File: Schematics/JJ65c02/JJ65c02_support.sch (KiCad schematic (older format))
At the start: 14 parts, among them SW1 RESET, U1 NE555, U2 74HC00, U3 74HC138, U4 74HC08, X1 1Mhz, X2 1.8Mhz

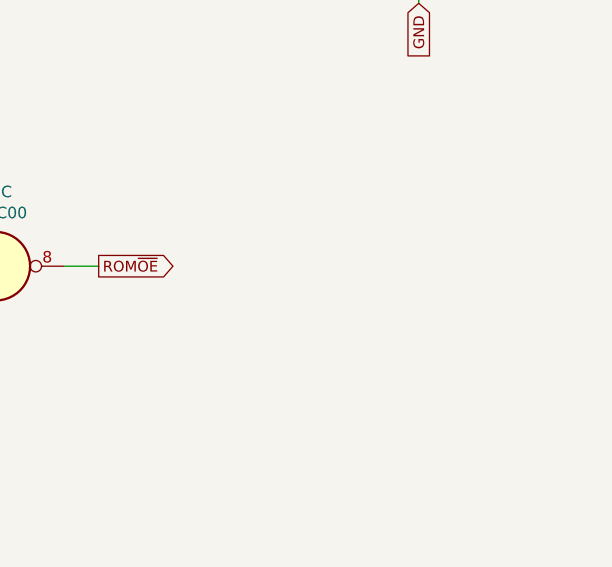
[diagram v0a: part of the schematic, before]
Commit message: Add in max232 board
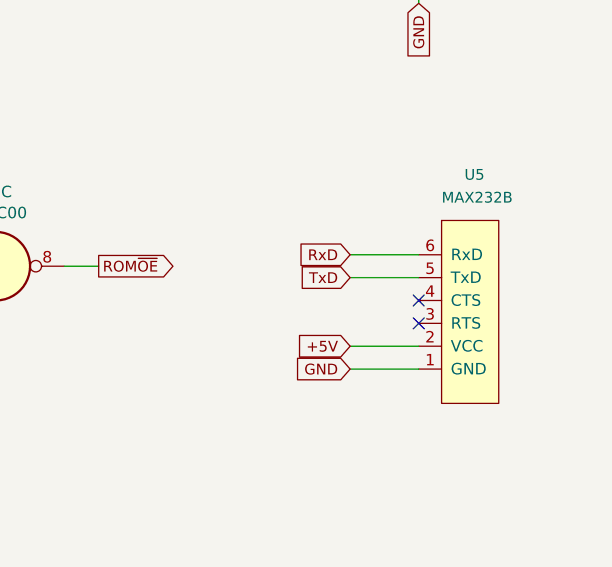
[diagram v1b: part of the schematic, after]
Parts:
- added U5: MAX232B, symbol 6502:MAX232B
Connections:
- net +5V: now also U5.2 (VCC)
- net GND: now also U5.1 (GND)
- new net RxD: U5.6 (RxD)
- new net TxD: U5.5 (TxD)
- no-connect marks 10 -> 12
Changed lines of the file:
@@
 Text Notes 1350 4550 0    98   ~ 0
 ~IRQ~ Logic Glue
+$Comp
+L 6502:MAX232B U5
+U 1 1 616302EB
+P 9350 4350
+F 0 "U5" V 10100 4050 47  0000 R CNN
+F 1 "MAX232B" V 10000 4150 47  0000 R CNN
+F 2 "" H 9350 4350 47  0001 C CNN
+F 3 "" H 9350 4350 47  0001 C CNN
+	1    9350 4350
+	0    -1   -1   0
+$EndComp
+Text GLabel 9150 3950 0    47   Input ~ 0
+RxD
+Text GLabel 9150 4050 0    47   Input ~ 0
+TxD
+Text GLabel 9150 4350 0    47   Input ~ 0
++5V
+Text GLabel 9150 4450 0    47   Input ~ 0
+GND
+Wire Wire Line
+	9150 3950 9450 3950
+Wire Wire Line
+	9150 4050 9450 4050
+Wire Wire Line
+	9150 4350 9450 4350
+Wire Wire Line
+	9150 4450 9450 4450
+NoConn ~ 9450 4150
+NoConn ~ 9450 4250
 Wire Bus Line
 	5000 2400 5000 3150

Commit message: Rough footprint and routing for max232 board
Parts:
- U5: footprint (none) -> TerminalBlock_TE-Connectivity:TerminalBlock_TE_282834-6_1x06_P2.54mm_Horizontal
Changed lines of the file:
@@
 F 0 "U5" V 10100 4050 47  0000 R CNN
 F 1 "MAX232B" V 10000 4150 47  0000 R CNN
-F 2 "" H 9350 4350 47  0001 C CNN
+F 2 "TerminalBlock_TE-Connectivity:TerminalBlock_TE_282834-6_1x06_P2.54mm_Horizontal" H 9350 4350 47  0001 C CNN
 F 3 "" H 9350 4350 47  0001 C CNN
 	1    9350 4350

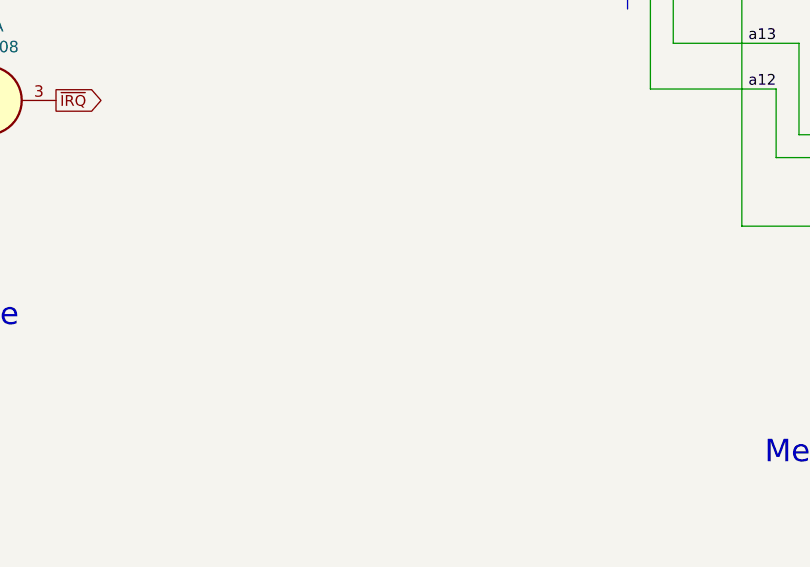
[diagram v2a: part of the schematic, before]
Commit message: Ensure mapping of power global labels to actual power rails.
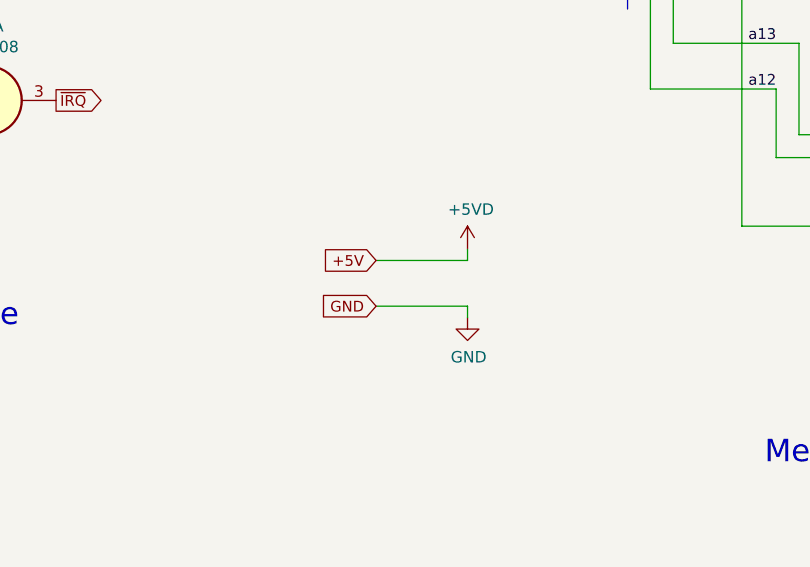
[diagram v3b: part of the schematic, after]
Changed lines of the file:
@@
 NoConn ~ 9450 4150
 NoConn ~ 9450 4250
+$Comp
+L power:+5VD #PWR?
+U 1 1 6160B5F2
+P 4300 4200
+F 0 "#PWR?" H 4300 4050 50  0001 C CNN
+F 1 "+5VD" H 4315 4373 50  0000 C CNN
+F 2 "" H 4300 4200 50  0001 C CNN
+F 3 "" H 4300 4200 50  0001 C CNN
+	1    4300 4200
+	1    0    0    -1
+$EndComp
+$Comp
+L power:GND #PWR?
+U 1 1 6160BF33
+P 4300 4500
+F 0 "#PWR?" H 4300 4250 50  0001 C CNN
+F 1 "GND" H 4305 4327 50  0000 C CNN
+F 2 "" H 4300 4500 50  0001 C CNN
+F 3 "" H 4300 4500 50  0001 C CNN
+	1    4300 4500
+	1    0    0    -1
+$EndComp
+Text GLabel 3900 4250 0    47   Input ~ 0
++5V
+Text GLabel 3900 4450 0    47   Input ~ 0
+GND
+Wire Wire Line
+	3900 4250 4300 4250
+Wire Wire Line
+	4300 4250 4300 4200
+Wire Wire Line
+	3900 4450 4300 4450
+Wire Wire Line
+	4300 4450 4300 4500
 Wire Bus Line
 	5000 2400 5000 3150

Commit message: Update schematic
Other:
- note added: "Memory Map:\n$0000 - $7fff RAM: 32k\n $0000 - $00ff RAM: Zero Page\n $0100 - $01ff RAM: Stack pointer (sp) / Page 1\n $0200 - $02ff RAM: miniOS system memory\n$8000 - $8fff IO: 4K\n $8010 - $801f ACIA\n $8020 - $802f VIA\n$9000 - $ffff ROM: 28K"
- note removed: "Memory Map:\n$0000 - $7fff RAM: 32k\n $0000 - $00ff RAM: Zero Page\n $0100 - $01ff RAM: Stack pointer (sp) / Page 1\n $0200 - $02ff RAM: miniOS system memory\n$8000 - $8fff IO: 4K\n$9000 - $ffff ROM: 28K"
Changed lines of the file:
@@
 Memory Map Logic Glue
 Text Notes 1050 7000 0    118  ~ 0
-Memory Map:\n$0000 - $7fff      RAM: 32k\n  $0000 - $00ff     RAM: Zero Page\n  $0100 - $01ff     RAM: Stack pointer (sp) / Page 1\n  $0200 - $02ff     RAM: miniOS system memory\n$8000 - $8fff      IO: 4K\n$9000 - $ffff      ROM: 28K
+Memory Map:\n$0000 - $7fff      RAM: 32k\n  $0000 - $00ff      RAM: Zero Page\n  $0100 - $01ff      RAM: Stack pointer (sp) / Page 1\n  $0200 - $02ff      RAM: miniOS system memory\n$8000 - $8fff      IO: 4K\n  $8010 - $801f     ACIA\n  $8020 - $802f     VIA\n$9000 - $ffff      ROM: 28K
 Text Notes 5200 700  0    98   ~ 0
 Support Schematics

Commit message: Update w/ latest schematics and datasheets. Fully on-board memory map and restart ckt
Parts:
- removed C1: 0.1uF, Capacitor_THT:C_Disc_D3.4mm_W2.1mm_P2.50mm, symbol Device:C
- U1: symbol 6502:NE555-Timer -> JJ65c02-rescue:NE555-Timer-6502
- U5: symbol 6502:MAX232B -> JJ65c02-rescue:MAX232B-6502
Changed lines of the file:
@@
 $EndDescr
 $Comp
-L 6502:NE555-Timer U1
+L JJ65c02-rescue:NE555-Timer-6502 U1
 U 1 1 5E17C676
 P 2500 1700
@@
 $EndComp
 Wire Wire Line
-	1600 2150 1600 2400
-Wire Wire Line
-	1600 2400 1750 2400
-Wire Wire Line
 	1750 2300 1750 2400
 Connection ~ 1750 2400
@@
 Wire Wire Line
 	2500 1300 2500 1000
-Connection ~ 1600 2400
-Wire Wire Line
-	1100 1000 1200 1000
-Connection ~ 1750 1000
-Wire Wire Line
-	1050 2400 1200 2400
-$Comp
-L Device:C C1
-U 1 1 5E7C431C
-P 1200 1700
-AR Path="/61660CAC/5E7C431C" Ref="C1"  Part="1"
-AR Path="/61610474/5E7C431C" Ref="C?"  Part="1"
-F 0 "C1" H 1315 1746 50  0000 L CNN
-F 1 "0.1uF" H 1315 1655 50  0000 L CNN
-F 2 "Capacitor_THT:C_Disc_D3.4mm_W2.1mm_P2.50mm" H 1238 1550 50  0001 C CNN
-F 3 "~" H 1200 1700 50  0001 C CNN
-	1    1200 1700
-	1    0    0    -1
-$EndComp
-Wire Wire Line
-	1200 1850 1200 2400
-Connection ~ 1200 2400
-Wire Wire Line
-	1200 2400 1600 2400
-Wire Wire Line
-	1200 1550 1200 1000
-Connection ~ 1200 1000
-Wire Wire Line
-	1200 1000 1750 1000
 $Comp
 L 74xx:74HC00 U2
@@
 Wire Wire Line
 	6750 3300 6350 3300
-Text GLabel 1100 1000 0    47   Input ~ 0
-+5V
-Text GLabel 1050 2400 0    47   Input ~ 0
+Text GLabel 1250 1000 0    47   Input ~ 0
++5V
+Text GLabel 1200 2400 0    47   Input ~ 0
 GND
 Text GLabel 9450 2850 3    47   Input ~ 0
@@
 ~IRQ~ Logic Glue
 $Comp
-L 6502:MAX232B U5
+L JJ65c02-rescue:MAX232B-6502 U5
 U 1 1 616302EB
 P 9350 4350
+AR Path="/616302EB" Ref="U5"  Part="1"
+AR Path="/61660CAC/616302EB" Ref="U5"  Part="1"
 F 0 "U5" V 10100 4050 47  0000 R CNN
 F 1 "MAX232B" V 10000 4150 47  0000 R CNN
@@
 Wire Wire Line
 	4300 4450 4300 4500
+Wire Wire Line
+	1250 1000 1750 1000
+Connection ~ 1750 1000
+Wire Wire Line
+	1200 2400 1600 2400
+Wire Wire Line
+	1600 2150 1600 2400
 Wire Bus Line
 	5000 2400 5000 3150
+Connection ~ 1600 2400
+Wire Wire Line
+	1600 2400 1750 2400
 $EndSCHEMATC

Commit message: Update schematics: pull down ckt was incorrect
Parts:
- U3: value 74HC138 -> 74AC138
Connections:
- net IO~CS: no longer U2.9
- net RAM~CS: now also U2.9
- net ROM~CE: no longer names the net of U2.3, U2.4
- net ROM~OE renamed ROM~CS
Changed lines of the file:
@@
 	5500 2500 5650 2500
-Wire Wire Line
-	6250 2400 6350 2400
 Wire Wire Line
 	5100 2900 5200 2900
@@
 Text GLabel 6400 2600 0    43   Input ~ 0
 CLK
-Wire Wire Line
-	6350 2400 6350 2100
-Connection ~ 6350 2400
-Wire Wire Line
-	6350 2400 6500 2400
 Text GLabel 4725 2550 2    35   BiDi ~ 0
 a[0..15]
@@
 RAM~CS
 Wire Wire Line
-	7100 2500 7300 2500
-Text GLabel 7300 2100 2    47   Output ~ 0
-ROM~CE
-Wire Wire Line
-	6350 2100 7300 2100
-Wire Wire Line
-	7300 2100 7300 2150
+	7100 2500 7200 2500
 Entry Wire Line
 	5000 3000 5100 3100
@@
 	5500 4100 5850 4100
 Text GLabel 8050 4000 2    47   Output ~ 0
-ROM~OE
+ROM~CS
 Wire Wire Line
 	6850 3600 7100 3600
@@
 	1    0    0    -1
 $EndComp
-Wire Wire Line
-	7100 3600 7100 3900
-Wire Wire Line
-	7100 3900 7300 3900
 Connection ~ 7100 3600
 Wire Wire Line
 	7100 3600 7300 3600
 Wire Wire Line
-	7100 3900 7100 4100
-Wire Wire Line
 	7100 4100 7300 4100
-Connection ~ 7100 3900
-Wire Wire Line
-	7900 4000 8050 4000
 NoConn ~ 6850 3700
 NoConn ~ 6850 3800
@@
 AR Path="/61610474/615D1D41" Ref="U?"  Part="1"
 F 0 "U3" H 6350 4681 50  0000 C CNN
-F 1 "74HC138" H 6350 4590 50  0000 C CNN
+F 1 "74AC138" H 6350 4590 50  0000 C CNN
 F 2 "Package_DIP:DIP-16_W7.62mm_Socket" H 6350 3900 50  0001 C CNN
 F 3 "http://www.ti.com/lit/gpn/sn74LS138" H 6350 3900 50  0001 C CNN
@@
 Wire Wire Line
 	1600 2150 1600 2400
+Connection ~ 1600 2400
+Wire Wire Line
+	1600 2400 1750 2400
+Wire Wire Line
+	6250 2400 6500 2400
+Wire Wire Line
+	8050 4000 7900 4000
+Wire Wire Line
+	7100 3600 7100 4100
+Wire Wire Line
+	7200 3900 7300 3900
+Wire Wire Line
+	7200 3900 7200 2500
 Wire Bus Line
 	5000 2400 5000 3150
-Connection ~ 1600 2400
-Wire Wire Line
-	1600 2400 1750 2400
+Connection ~ 7200 2500
+Wire Wire Line
+	7200 2500 7300 2500
 $EndSCHEMATC

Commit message: Updates w/ newer schematics and layout
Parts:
- added D1: LED, symbol Device:LED
- added R?: 220, Resistor_THT:R_Axial_DIN0207_L6.3mm_D2.5mm_P7.62mm_Horizontal, symbol Device:R
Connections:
- net +5V: now also R?.1
- net GND: now also D1.1 (K)
- new net: D1.2 (A), R?.2
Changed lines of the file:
@@
 Wire Wire Line
 	7200 3900 7200 2500
-Wire Bus Line
-	5000 2400 5000 3150
 Connection ~ 7200 2500
 Wire Wire Line
 	7200 2500 7300 2500
+$Comp
+L Device:LED D1
+U 1 1 61721221
+P 8150 1450
+F 0 "D1" V 8189 1332 50  0000 R CNN
+F 1 "LED" V 8098 1332 50  0000 R CNN
+F 2 "" H 8150 1450 50  0001 C CNN
+F 3 "~" H 8150 1450 50  0001 C CNN
+	1    8150 1450
+	0    -1   -1   0
+$EndComp
+$Comp
+L Device:R R?
+U 1 1 617239C1
+P 8150 1150
+AR Path="/61660CAC/617239C1" Ref="R?"  Part="1"
+AR Path="/61610474/617239C1" Ref="R?"  Part="1"
+F 0 "R?" V 8050 1150 50  0000 C CNN
+F 1 "220" V 8150 1150 50  0000 C CNN
+F 2 "Resistor_THT:R_Axial_DIN0207_L6.3mm_D2.5mm_P7.62mm_Horizontal" V 8080 1150 50  0001 C CNN
+F 3 "~" H 8150 1150 50  0001 C CNN
+	1    8150 1150
+	1    0    0    -1
+$EndComp
+Text GLabel 7800 1000 0    47   Input ~ 0
++5V
+Text GLabel 7800 1700 0    47   Input ~ 0
+GND
+Wire Wire Line
+	7800 1000 8150 1000
+Wire Wire Line
+	7800 1700 8150 1700
+Wire Wire Line
+	8150 1700 8150 1600
+Wire Bus Line
+	5000 2400 5000 3150
 $EndSCHEMATC

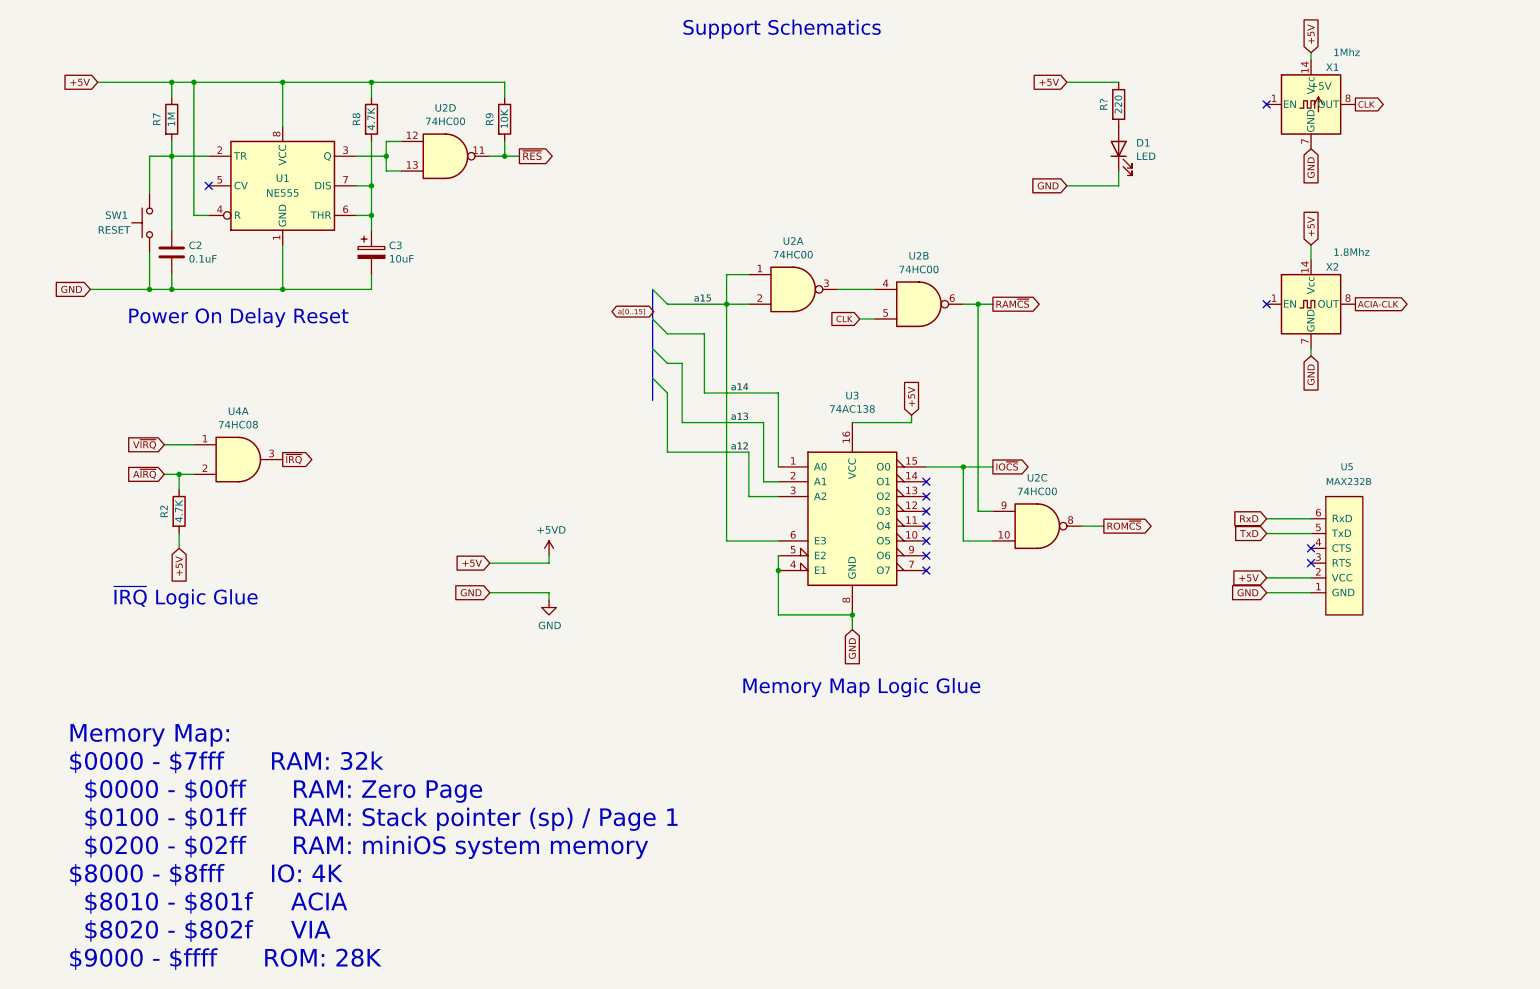
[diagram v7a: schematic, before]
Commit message: Some updates:   o emulator includes serial term   o sep LCD and VIA inits   o Add 2nd VIA and sound amp ckt
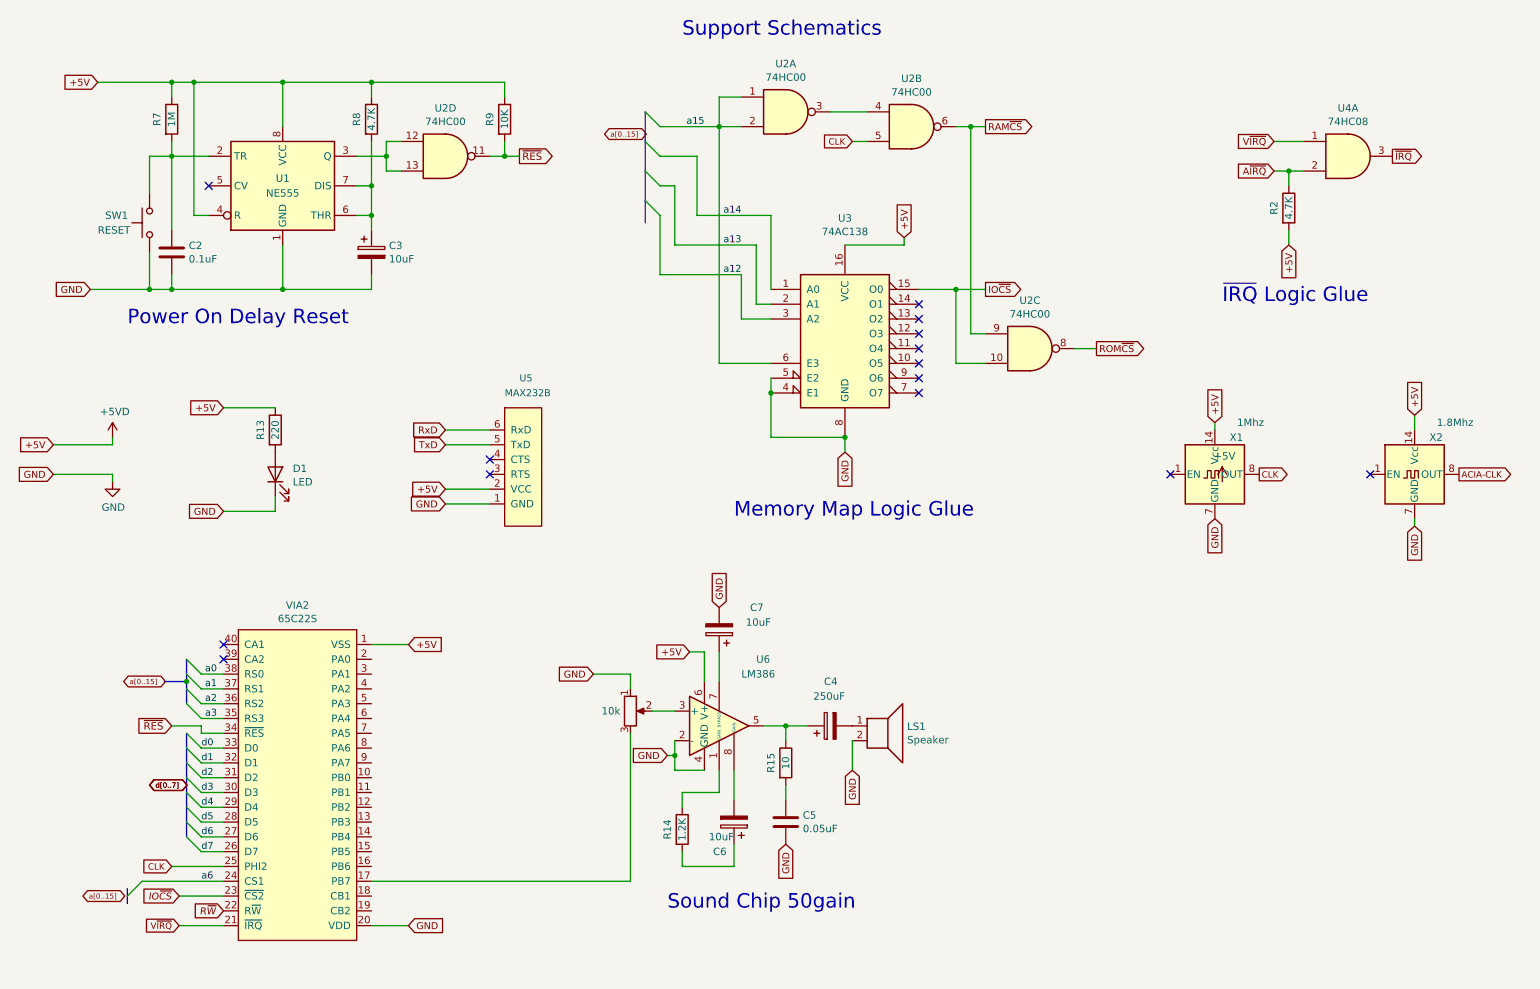
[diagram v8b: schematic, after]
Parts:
- added C4: 250uF, Capacitor_THT:C_Disc_D3.4mm_W2.1mm_P2.50mm, symbol Device:CP
- added C5: 0.05uF, Capacitor_THT:C_Disc_D3.4mm_W2.1mm_P2.50mm, symbol Device:C
- added C6, C7: 10uF, Capacitor_THT:C_Disc_D3.4mm_W2.1mm_P2.50mm, symbol Device:CP
- added LS1: Speaker, symbol Device:Speaker
- added R14: 1.2K, Resistor_THT:R_Axial_DIN0207_L6.3mm_D2.5mm_P7.62mm_Horizontal, symbol Device:R
- added R15: 10, Resistor_THT:R_Axial_DIN0207_L6.3mm_D2.5mm_P7.62mm_Horizontal, symbol Device:R
- added RV2: 10k, Potentiometer_THT:Potentiometer_Bourns_3339P_Vertical, symbol Device:R_POT
- added U6: LM386, symbol Amplifier_Audio:LM386
- added VIA2: 65C22S, Package_DIP:DIP-40_W15.24mm_Socket, symbol 6502:65C22S
- gave numbers to parts that had none: 1
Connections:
- net +5V: now also U6.6 (V+), VIA2.1 (VSS)
- net CLK: now also VIA2.25 (PHI2)
- net GND: now also C5.2, C7.2, LS1.2, RV2.1, U6.2 (-), U6.4 (GND), VIA2.20 (VDD)
- net IO~CS: now also VIA2.23 (~CS2)
- net V~IRQ: now also VIA2.21 (~IRQ)
- net ~RES: now also VIA2.34 (~RES)
- new net: RV2.3, VIA2.17 (PB7)
- new net: R14.1, U6.1 (GAIN)
- new net: RV2.2, U6.3 (+)
- new net: C4.1, R15.1, U6.5
- new net: C7.1, U6.7 (BYPASS)
- new net: C6.2, U6.8 (GAIN)
- new net: C4.2, LS1.1
- new net: C5.1, R15.2
- new net: C6.1, R14.2
- new net R~W: VIA2.22 (R~W)
- new net a0: VIA2.38 (RS0)
- new net a1: VIA2.37 (RS1)
- new net a2: VIA2.36 (RS2)
- new net a3: VIA2.35 (RS3)
- new net a6: VIA2.24 (CS1)
- new net d0: VIA2.33 (D0)
- new net d1: VIA2.32 (D1)
- new net d2: VIA2.31 (D2)
- new net d3: VIA2.30 (D3)
- new net d4: VIA2.29 (D4)
- new net d5: VIA2.28 (D5)
- new net d6: VIA2.27 (D6)
- new net d7: VIA2.26 (D7)
- no-connect marks 12 -> 14
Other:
- note added: "Sound Chip 50gain"
- note removed: "Memory Map:\n$0000 - $7fff RAM: 32k\n $0000 - $00ff RAM: Zero Page\n $0100 - $01ff RAM: Stack pointer (sp) / Page 1\n $0200 - $02ff RAM: miniOS system memory\n$8000 - $8fff IO: 4K\n $8010 - $801f ACIA\n $8020 - $802f VIA\n$9000 - $ffff ROM: 28K"
- moved on the sheet: D1, R13, R2, U2A, U2B, U2C, U3, U4A, U5, X1, X2
